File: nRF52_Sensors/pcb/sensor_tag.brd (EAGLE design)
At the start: 36.5 x 26.7 mm, 5 parts

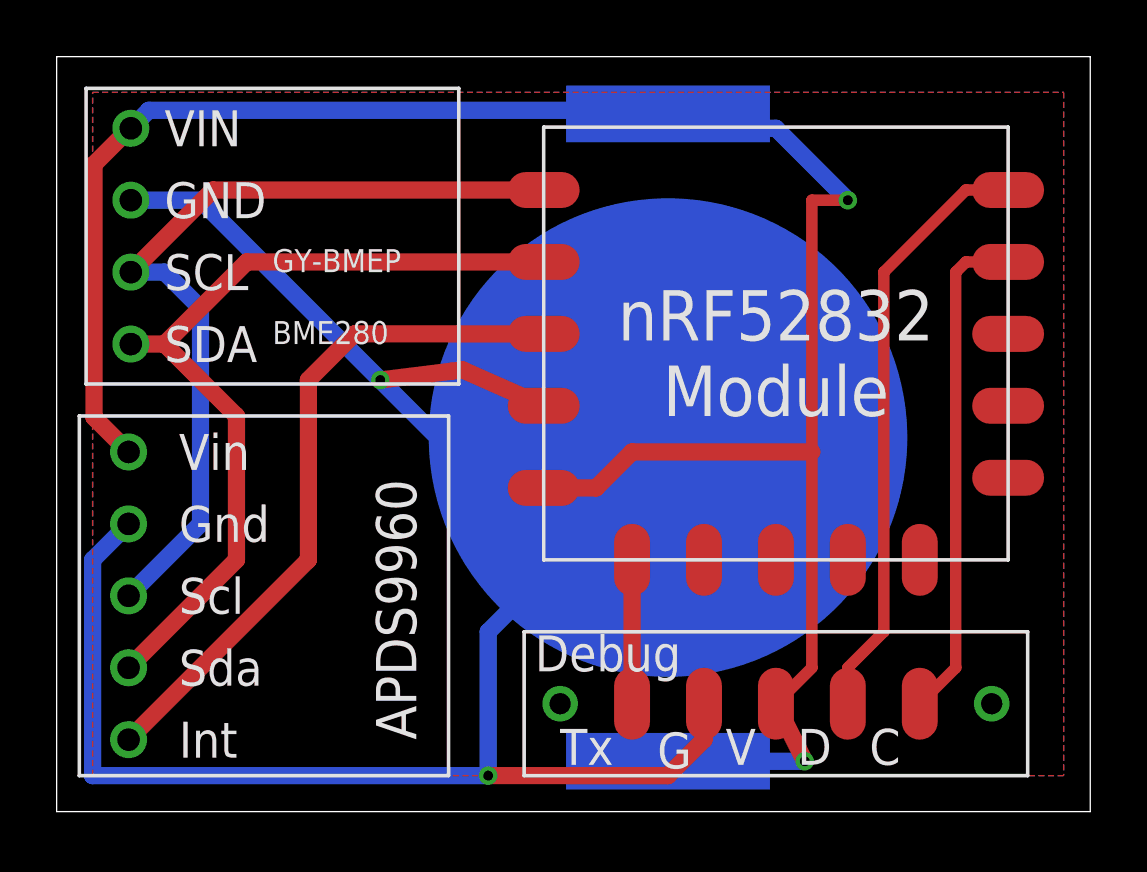
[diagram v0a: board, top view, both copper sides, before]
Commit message: shifted APDS module to support MPU add in gnd
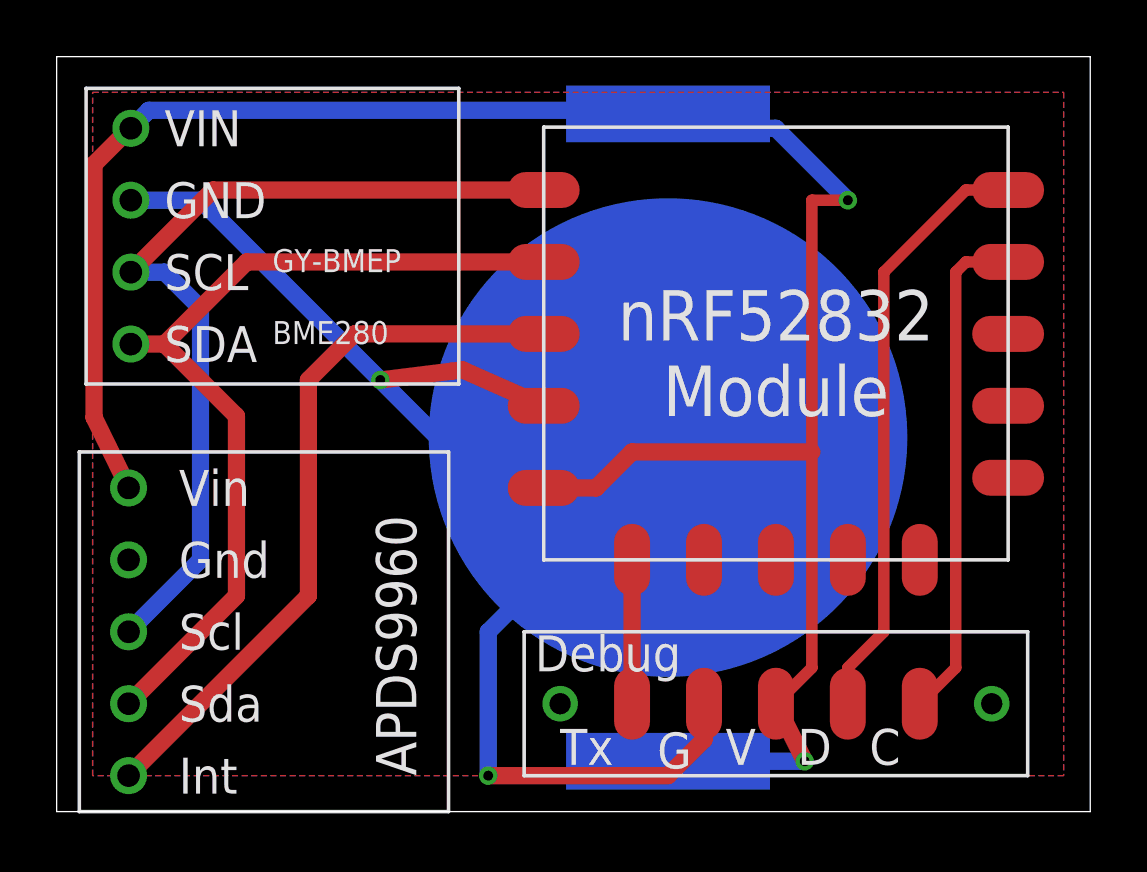
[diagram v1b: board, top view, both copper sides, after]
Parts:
- moved U$2 1.27 mm to (2.54, 6.35)
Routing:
- net GND: track 75.1 -> 51.8 mm
- net SDA: track 29.9 -> 31.2 mm
- net SCL: track 30.0 -> 31.2 mm
- net INT: track 24.3 -> 25.6 mm
- net VCC: track 76.0 -> 77.1 mm
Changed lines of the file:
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@@
 <elements>
 <element name="U$1" library="GY-BMEP" package="GY-BMEP-NOHOLE" value="GY-BMEPGY-BMEP-NOHOLE" x="7.62" y="20.32"/>
-<element name="U$2" library="APDS9960" package="APDS9960-FULL" value="APDS9960_MODULEAPDS9960-FULL" x="2.54" y="7.62"/>
+<element name="U$2" library="APDS9960" package="APDS9960-FULL" value="APDS9960_MODULEAPDS9960-FULL" x="2.54" y="6.35"/>
 <element name="U$3" library="nRF52832_module" package="NRF52832_MOD_SMALL" value="NRF52832_MODULENRF52832_MOD_SMALL" x="25.4" y="17.78"/>
 <element name="U$4" library="cr2032" package="CR2032_SMD" value="CR2032" x="21.59" y="13.208" rot="MR270"/>
@@
 <wire x1="2.62" y1="21.59" x2="5.08" y2="21.59" width="0.6096" layer="16"/>
 <wire x1="5.08" y1="21.59" x2="11.43" y2="15.24" width="0.6096" layer="16"/>
-<wire x1="2.54" y1="10.16" x2="1.27" y2="8.89" width="0.6096" layer="16"/>
-<wire x1="1.27" y1="8.89" x2="1.27" y2="1.27" width="0.6096" layer="16"/>
-<wire x1="1.27" y1="1.27" x2="15.24" y2="1.27" width="0.6096" layer="16"/>
 <wire x1="15.24" y1="1.27" x2="15.24" y2="6.35" width="0.6096" layer="16"/>
 <wire x1="15.24" y1="6.35" x2="20.32" y2="11.43" width="0.6096" layer="16"/>
@@
 <contactref element="U$2" pad="VIN"/>
 <contactref element="U$1" pad="VIN"/>
-<wire x1="2.54" y1="12.7" x2="1.3208" y2="13.9192" width="0.6096" layer="1"/>
+<wire x1="2.54" y1="11.43" x2="1.3208" y2="13.9192" width="0.6096" layer="1"/>
 <wire x1="1.3208" y1="13.9192" x2="1.3208" y2="22.86" width="0.6096" layer="1"/>
 <wire x1="1.3208" y1="22.86" x2="2.5908" y2="24.13" width="0.6096" layer="1"/>
@@
 <contactref element="U$1" pad="SCL"/>
 <contactref element="U$2" pad="SCL"/>
-<wire x1="2.54" y1="7.62" x2="5.08" y2="10.16" width="0.6096" layer="16"/>
-<wire x1="5.08" y1="10.16" x2="5.08" y2="17.78" width="0.6096" layer="16"/>
+<wire x1="2.54" y1="6.35" x2="5.08" y2="8.89" width="0.6096" layer="16"/>
+<wire x1="5.08" y1="8.89" x2="5.08" y2="17.78" width="0.6096" layer="16"/>
 <wire x1="3.81" y1="19.05" x2="5.08" y2="17.78" width="0.6096" layer="16"/>
 <wire x1="2.62" y1="19.05" x2="3.81" y2="19.05" width="0.6096" layer="16"/>
@@
 <contactref element="U$2" pad="SDA"/>
 <contactref element="U$1" pad="SDA"/>
-<wire x1="2.54" y1="5.08" x2="6.35" y2="8.89" width="0.6096" layer="1"/>
-<wire x1="6.35" y1="8.89" x2="6.35" y2="13.97" width="0.6096" layer="1"/>
+<wire x1="2.54" y1="3.81" x2="6.35" y2="7.62" width="0.6096" layer="1"/>
+<wire x1="6.35" y1="7.62" x2="6.35" y2="13.97" width="0.6096" layer="1"/>
 <wire x1="6.35" y1="13.97" x2="3.81" y2="16.51" width="0.6096" layer="1"/>
 <wire x1="2.62" y1="16.51" x2="2.54" y2="16.51" width="0.6096" layer="1"/>
@@
 <contactref element="U$3" pad="P0_31"/>
 <contactref element="U$2" pad="INT"/>
-<wire x1="2.54" y1="2.54" x2="8.89" y2="8.89" width="0.6096" layer="1"/>
-<wire x1="8.89" y1="8.89" x2="8.89" y2="15.24" width="0.6096" layer="1"/>
+<wire x1="2.54" y1="1.27" x2="8.89" y2="7.62" width="0.6096" layer="1"/>
+<wire x1="8.89" y1="7.62" x2="8.89" y2="15.24" width="0.6096" layer="1"/>
 <wire x1="8.89" y1="15.24" x2="10.52" y2="16.87" width="0.6096" layer="1"/>
 <wire x1="10.52" y1="16.87" x2="17.2" y2="16.87" width="0.6096" layer="1"/>
